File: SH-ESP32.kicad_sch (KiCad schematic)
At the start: 0 parts

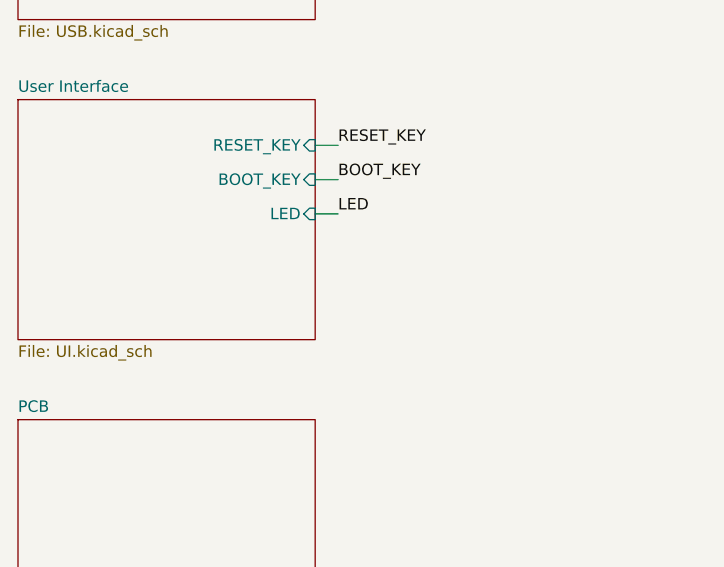
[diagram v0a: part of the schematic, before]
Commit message: Go back to ISO1050 for CAN transceiver
Also add CAN RX and TX LEDs and beef up buck capacitors
as much as space allows.
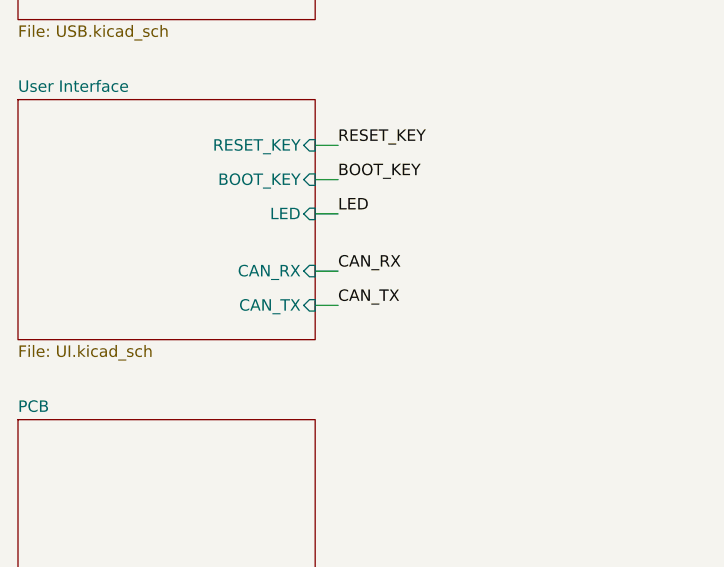
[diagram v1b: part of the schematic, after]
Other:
- sheet User Interface ports: added CAN_RX, CAN_TX; removed none
- company: Hat Labs Ltd -> Hat Labs Oy
- title: Sailor Hat with ESP32 -> SH-ESP32
